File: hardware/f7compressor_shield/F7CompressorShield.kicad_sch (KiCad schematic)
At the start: 14 parts, among them CN10 NUCLEO Zio CN10 (17x2), CN7 NUCLEO Zio CN7 (10x2), CN8 NUCLEO Zio CN8 (8x2), CN9 NUCLEO Zio CN9 (15x2), J1 LCD P1/P2 (ILI9341+XPT2046), J2 Relay module J1 (VCC/GND/IN1-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, J5 4-20mA pressure loop field te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, J6 5VDC power input, SW1 MTS-1 (OIL_SW simulate), SW2 MTS-1 (ESTOP simulate), SW3 MTS-1 (motor RUN_SENSE simula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, U1 NUCLEO-H723ZG Morpho (CN11/CN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

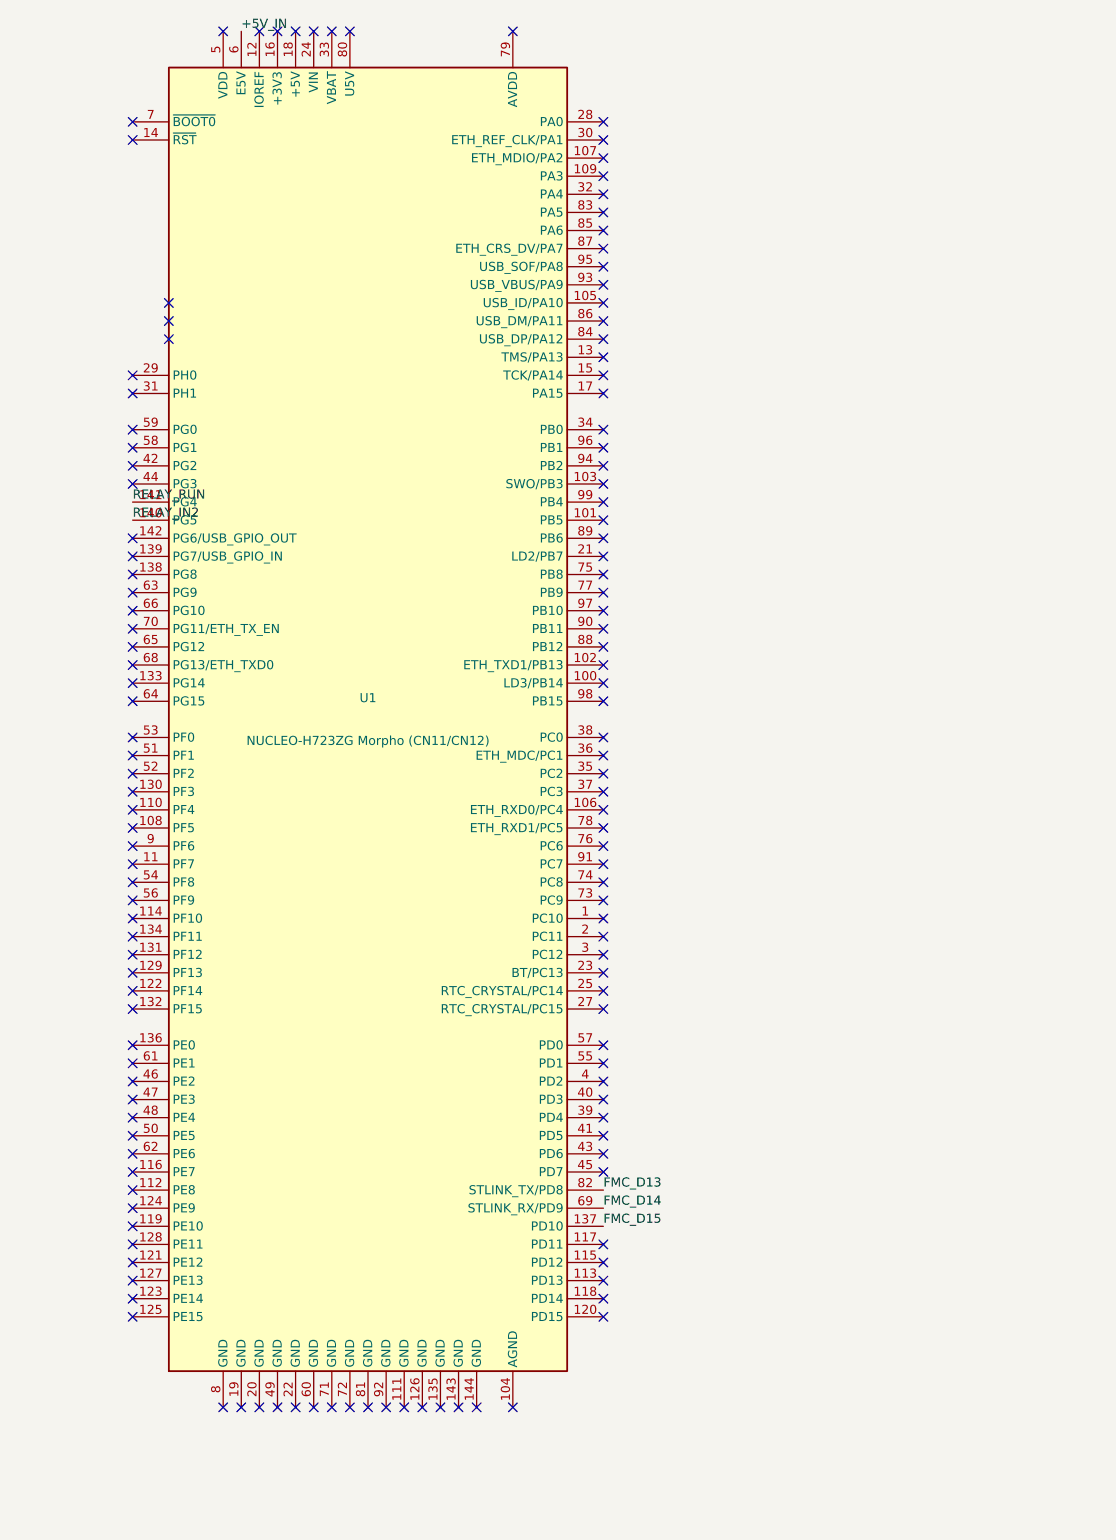
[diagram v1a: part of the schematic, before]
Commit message: Split Morpho U1 into real CN11/CN12 connectors; fix place_mirrored() offset bug
CN11/CN12 were previously one combined ST footprint (148 pads, 8 more
than the real 140-pin total) representing two physically separate
connectors. Replaced with two separate 35x2 parts -- same footprint
family already pin-1-verified for CN7-CN10 -- using real pin numbers
from ST UM1974 Table 21, cross-checked against CLAUDE.md (all 6 signals
used here matched exactly).

While placing them, found that place_mirrored() was landing pad 1 one
full pin pitch (2.54mm) away from its intended position on every
connector it had touched (CN7-CN10, J1), not just the new ones -- the
hand-mirror step doesn't move the footprint's own anchor, so a naive
SetPosition(pos_mm) put pad 1 at pos_mm - 2.54mm instead of at pos_mm.
Fixed the function to solve for the anchor position that puts pad 1
exactly on target, and reverified all six mirrored connectors land
correctly.

Net effect: DRC findings dropped from 137 to 26 (splitting the combined
footprint removed most of its courtyard overlap with the Zio headers).
Re-routed and fixed the resulting clearance violations with verified
local detours (checked against pads and tracks, not just pads).

ERC clean, DRC 0 unconnected / 0 clearance violations.

Co-Authored-By: Claude Sonnet 5 <noreply@anthropic.com>
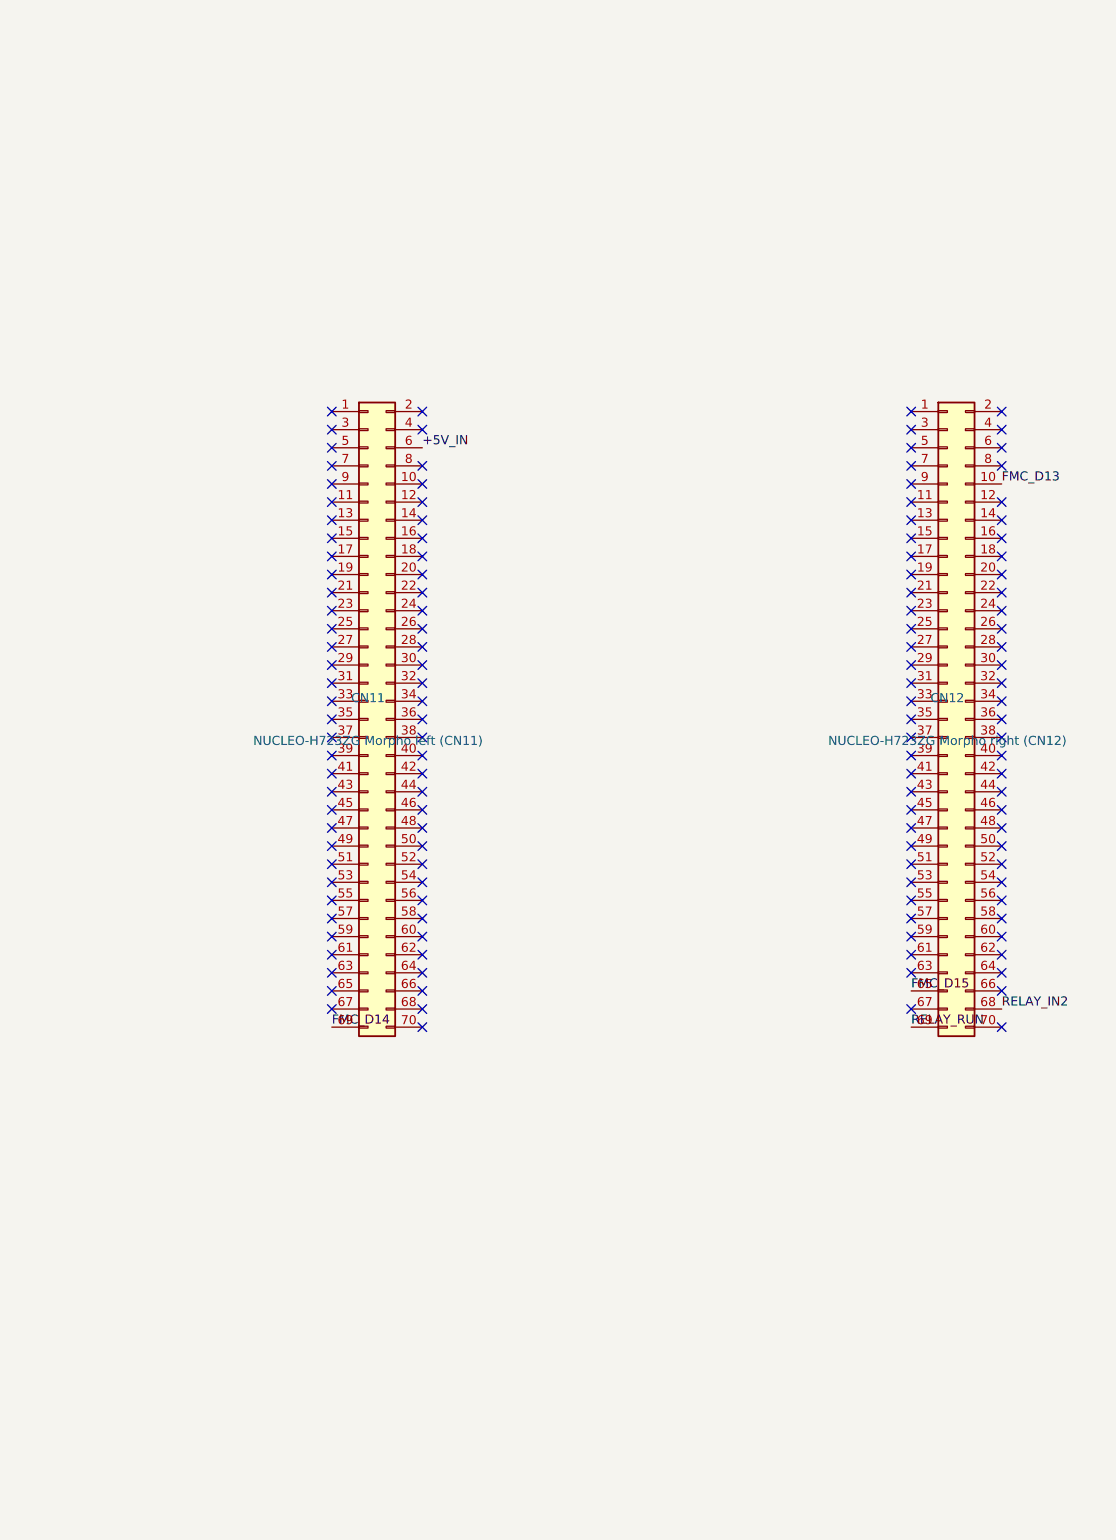
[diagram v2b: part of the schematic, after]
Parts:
- removed U1: NUCLEO-H723ZG Morpho (CN11/CN12), Module:ST_Morpho_Connector_144_STLink, symbol MCU_Module:NUCLEO144-F429ZI
- added CN11: NUCLEO-H723ZG Morpho left (CN11), Connector_PinSocket_2.54mm:PinSocket_2x35_P2.54mm_Vertical, symbol Connector_Generic:Conn_02x35_Odd_Even
- added CN12: NUCLEO-H723ZG Morpho right (CN12), Connector_PinSocket_2.54mm:PinSocket_2x35_P2.54mm_Vertical, symbol Connector_Generic:Conn_02x35_Odd_Even
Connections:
- net +5V_IN: now also CN11.6 (Pin_6)
- net FMC_D13: now also CN12.10 (Pin_10)
- net FMC_D14: now also CN11.69 (Pin_69)
- net FMC_D15: now also CN12.65 (Pin_65)
- net RELAY_IN2: now also CN12.68 (Pin_68)
- net RELAY_RUN: now also CN12.69 (Pin_69)
- no-connect marks 209 -> 205

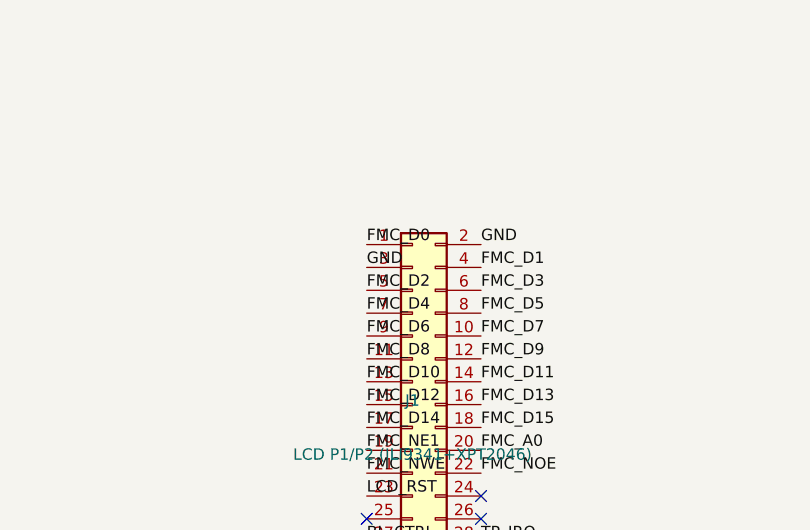
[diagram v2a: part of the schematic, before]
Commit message: Fix J1 LCD header pin 1/3 swap; correct wiring_diagram.html to match
Checked J1 against the LCD module's own manufacturer schematic
(read pin-by-pin via exact PDF text coordinates) and found pin 1 is
DC-5V (required power), not FMC_D0 -- the data bus actually starts
at pin 3, which this project (and wiring_diagram.html) had as GND.
Every other pin (4-34) already matched the real schematic exactly,
so this was isolated to the first two positions. Confirmed nothing
is physically wired to the LCD yet, so this never reached hardware.

Fixed J1's net assignment (pin1->+5V, pin3->FMC_D0) and the same
error in wiring_diagram.html, which previously didn't document the
LCD's real 5V power pin at all.

Re-routed after the pin change. One new clearance violation (a
BL_CTRL via packed in with CN12 pads and 5 other FMC nets) had no
valid position for a standard 0.6mm via anywhere within 0.8mm -- an
attempted F.Cu-only reroute around it looked clean until DRC caught
a true segment crossing my distance-based checker had missed (fixed
the checker, but the simpler and correct fix was just shrinking both
vias to 0.5mm, the board's declared minimum, at their original
positions).

ERC clean, DRC 0 unconnected / 0 clearance violations.

Co-Authored-By: Claude Sonnet 5 <noreply@anthropic.com>
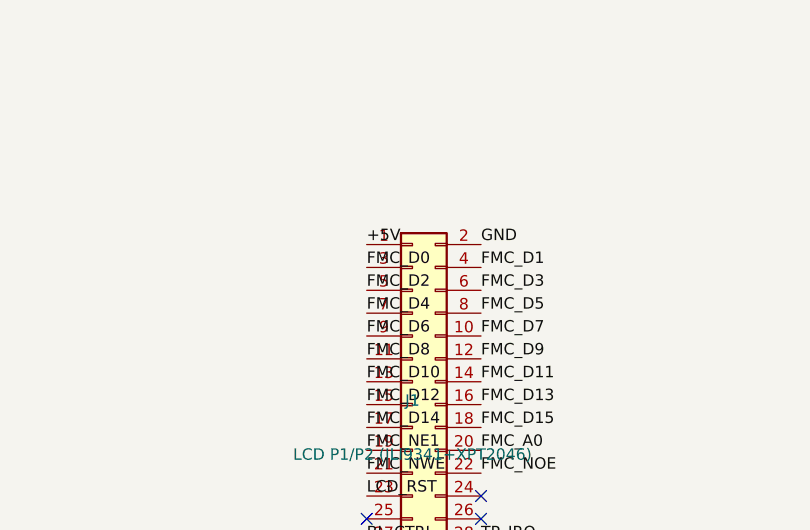
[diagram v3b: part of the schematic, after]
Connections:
- net +5V: now also J1.1 (Pin_1)
- net FMC_D0: now also J1.3 (Pin_3); no longer J1.1 (Pin_1)
- net GND: no longer J1.3 (Pin_3)
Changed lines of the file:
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@@
 		(effects (font (size 1.27 1.27)) (justify left bottom))
 	)
-	(label "FMC_D0"
+	(label "+5V"
 		(at 254 -20.32 0)
 		(effects (font (size 1.27 1.27)) (justify left bottom))
@@
 		(effects (font (size 1.27 1.27)) (justify left bottom))
 	)
-	(label "GND"
+	(label "FMC_D0"
 		(at 254 -17.78 0)
 		(effects (font (size 1.27 1.27)) (justify left bottom))

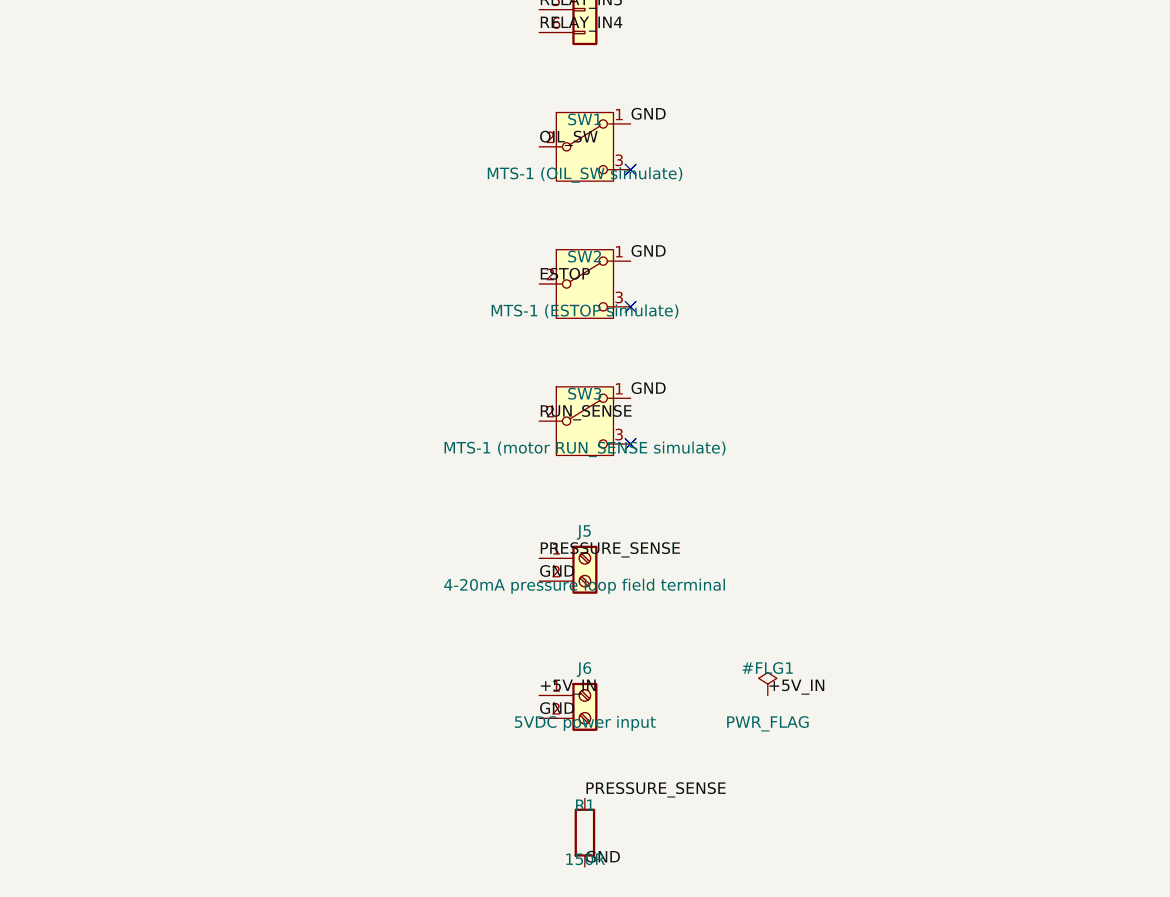
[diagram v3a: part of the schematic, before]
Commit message: Use real part numbers for J5/J6 and SW1-3; add generic switch 3D model
J5 and J6 now both use the exact KiCad-bundled footprint for Phoenix
Contact 1727010 (MKDS 1/2-3,81), replacing the generic MX126 placeholder.
SW1-3 updated to the real part, Dailywell 1MS1T1B1M1QES-5 -- confirmed
pin spacing (4.70mm) already matched the existing custom footprint
exactly. Its 6.35mm mounting bushing is nearly as wide as the whole
switch body, so it was left off the PCB footprint (strong evidence it
mounts through an enclosure panel, not the board).

Added a generic placeholder 3D model (3dmodels/SW_MTS1_generic.wrl) for
the switches, sized to the real part's body envelope, since no bundled
or downloadable model exists. Found and fixed a real scaling bug while
attaching it: KiCad interprets raw VRML coordinates at a fixed 2.54
scale (mm per 0.1in) regardless of the file's actual units. The correct
factor (1/2.54) was found by pixel-measuring the rendered model against
the footprint's own known pad pitch, not guessed -- an initial attempt
using the inches-to-mm factor (1/25.4) undershot by 10x.

Re-routed after both changes. ERC clean, DRC 0 unconnected / 0 clearance
violations.

Co-Authored-By: Claude Sonnet 5 <noreply@anthropic.com>
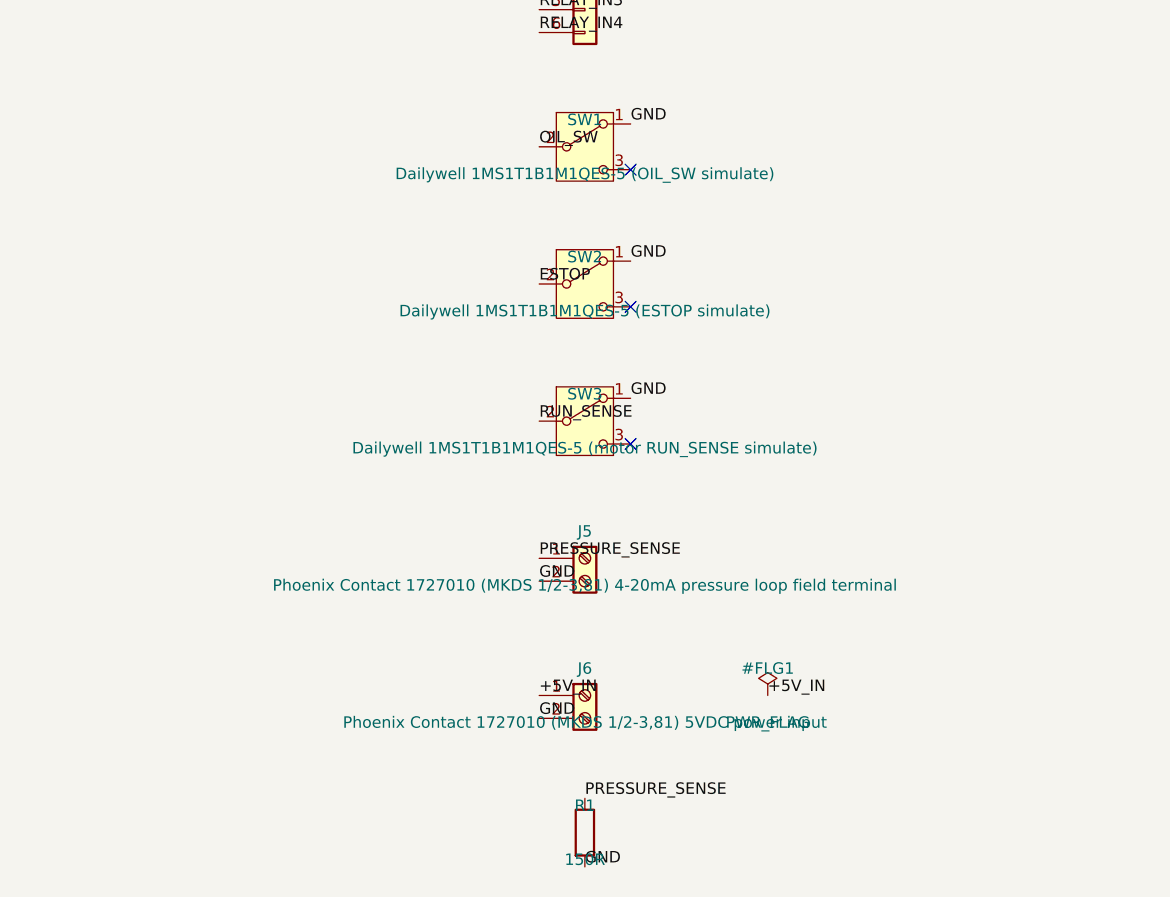
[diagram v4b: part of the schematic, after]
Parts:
- J5: value 4-20mA pressure loop field terminal -> Phoenix Contact 1727010 (MKDS 1/2-3,81) 4-20mA pressure loop field terminal; footprint TerminalBlock:TerminalBlock_MaiXu_MX126-5.0-02P_1x02_P5.00mm -> TerminalBlock_Phoenix:TerminalBlock_Phoenix_MKDS-1-2-3.81_1x02_P3.81mm_Horizontal
- J6: value 5VDC power input -> Phoenix Contact 1727010 (MKDS 1/2-3,81) 5VDC power input; footprint TerminalBlock:TerminalBlock_MaiXu_MX126-5.0-02P_1x02_P5.00mm -> TerminalBlock_Phoenix:TerminalBlock_Phoenix_MKDS-1-2-3.81_1x02_P3.81mm_Horizontal
- SW1: value MTS-1 (OIL_SW simulate) -> Dailywell 1MS1T1B1M1QES-5 (OIL_SW simulate)
- SW2: value MTS-1 (ESTOP simulate) -> Dailywell 1MS1T1B1M1QES-5 (ESTOP simulate)
- SW3: value MTS-1 (motor RUN_SENSE simulate) -> Dailywell 1MS1T1B1M1QES-5 (motor RUN_SENSE simulate)
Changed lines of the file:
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@@
 			(effects (font (size 1.27 1.27)))
 		)
-		(property "Value" "MTS-1 (OIL_SW simulate)"
+		(property "Value" "Dailywell 1MS1T1B1M1QES-5 (OIL_SW simulate)"
 			(at 259.08 112.22 0)
 			(effects (font (size 1.27 1.27)))
@@
 			(effects (font (size 1.27 1.27)))
 		)
-		(property "Value" "MTS-1 (ESTOP simulate)"
+		(property "Value" "Dailywell 1MS1T1B1M1QES-5 (ESTOP simulate)"
 			(at 259.08 127.46 0)
 			(effects (font (size 1.27 1.27)))
@@
 			(effects (font (size 1.27 1.27)))
 		)
-		(property "Value" "MTS-1 (motor RUN_SENSE simulate)"
+		(property "Value" "Dailywell 1MS1T1B1M1QES-5 (motor RUN_SENSE simulate)"
 			(at 259.08 142.7 0)
 			(effects (font (size 1.27 1.27)))
@@
 			(effects (font (size 1.27 1.27)))
 		)
-		(property "Value" "4-20mA pressure loop field terminal"
+		(property "Value" "Phoenix Contact 1727010 (MKDS 1/2-3,81) 4-20mA pressure loop field terminal"
 			(at 259.08 157.94 0)
 			(effects (font (size 1.27 1.27)))
 		)
-		(property "Footprint" "TerminalBlock:TerminalBlock_MaiXu_MX126-5.0-02P_1x02_P5.00mm"
+		(property "Footprint" "TerminalBlock_Phoenix:TerminalBlock_Phoenix_MKDS-1-2-3.81_1x02_P3.81mm_Horizontal"
 			(at 259.08 154.94 0)
 			(effects (font (size 1.27 1.27)) (hide yes))
@@
 			(effects (font (size 1.27 1.27)))
 		)
-		(property "Value" "5VDC power input"
+		(property "Value" "Phoenix Contact 1727010 (MKDS 1/2-3,81) 5VDC power input"
 			(at 259.08 173.18 0)
 			(effects (font (size 1.27 1.27)))
 		)
-		(property "Footprint" "TerminalBlock:TerminalBlock_MaiXu_MX126-5.0-02P_1x02_P5.00mm"
+		(property "Footprint" "TerminalBlock_Phoenix:TerminalBlock_Phoenix_MKDS-1-2-3.81_1x02_P3.81mm_Horizontal"
 			(at 259.08 170.18 0)
 			(effects (font (size 1.27 1.27)) (hide yes))
